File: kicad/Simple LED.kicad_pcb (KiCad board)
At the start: 2 copper layers, 100 x 60 mm, 3 parts, among them J1 Conn_01x02_Pin

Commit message: kicad schematic, 3d viewer, and files
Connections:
- net Net-(D1-K) renamed GND
- net Net-(J1-Pin_1) renamed +5V
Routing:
- added copper zone on B.Cu, net GND
- removed copper zone on B.Cu, net (none)
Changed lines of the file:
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@@
 		(tenting front back)
 		(pcbplotparams
-			(layerselection 0x00000000_00000000_55555555_5755f5ff)
+			(layerselection 0x00000000_00000000_55555555_575555ff)
 			(plot_on_all_layers_selection 0x00000000_00000000_00000000_00000000)
 			(disableapertmacros no)
@@
 			(sketchdnponfab yes)
 			(crossoutdnponfab yes)
-			(subtractmaskfromsilk no)
+			(subtractmaskfromsilk yes)
 			(outputformat 1)
 			(mirror no)
-			(drillshape 1)
+			(drillshape 0)
 			(scaleselection 1)
-			(outputdirectory "")
+			(outputdirectory "gerbers")
 		)
 	)
 	(net 0 "")
 	(net 1 "Net-(D1-A)")
-	(net 2 "Net-(D1-K)")
-	(net 3 "Net-(J1-Pin_1)")
+	(net 2 "GND")
+	(net 3 "+5V")
 	(footprint "Resistor_THT:R_Axial_DIN0617_L17.0mm_D6.0mm_P20.32mm_Horizontal"
 		(layer "F.Cu")
@@
 			(layers "*.Cu" "*.Mask")
 			(remove_unused_layers no)
-			(net 3 "Net-(J1-Pin_1)")
+			(net 3 "+5V")
 			(pintype "passive")
 		)
@@
 			(layers "*.Cu" "*.Mask")
 			(remove_unused_layers no)
-			(net 3 "Net-(J1-Pin_1)")
+			(net 3 "+5V")
 			(pinfunction "Pin_1")
 			(pintype "passive")
@@
 			(layers "*.Cu" "*.Mask")
 			(remove_unused_layers no)
-			(net 2 "Net-(D1-K)")
+			(net 2 "GND")
 			(pinfunction "Pin_2")
 			(pintype "passive")
@@
 			(layers "*.Cu" "*.Mask")
 			(remove_unused_layers no)
-			(net 2 "Net-(D1-K)")
+			(net 2 "GND")
 			(pinfunction "K")
 			(pintype "passive")
@@
 	)
 	(zone
-		(net 0)
-		(net_name "")
+		(net 2)
+		(net_name "GND")
 		(layer "B.Cu")
 		(hatch edge 0.5)
@@
 			(thermal_gap 0.5)
 			(thermal_bridge_width 0.5)
-			(island_removal_mode 1)
-			(island_area_min 10)
 		)
 		(polygon

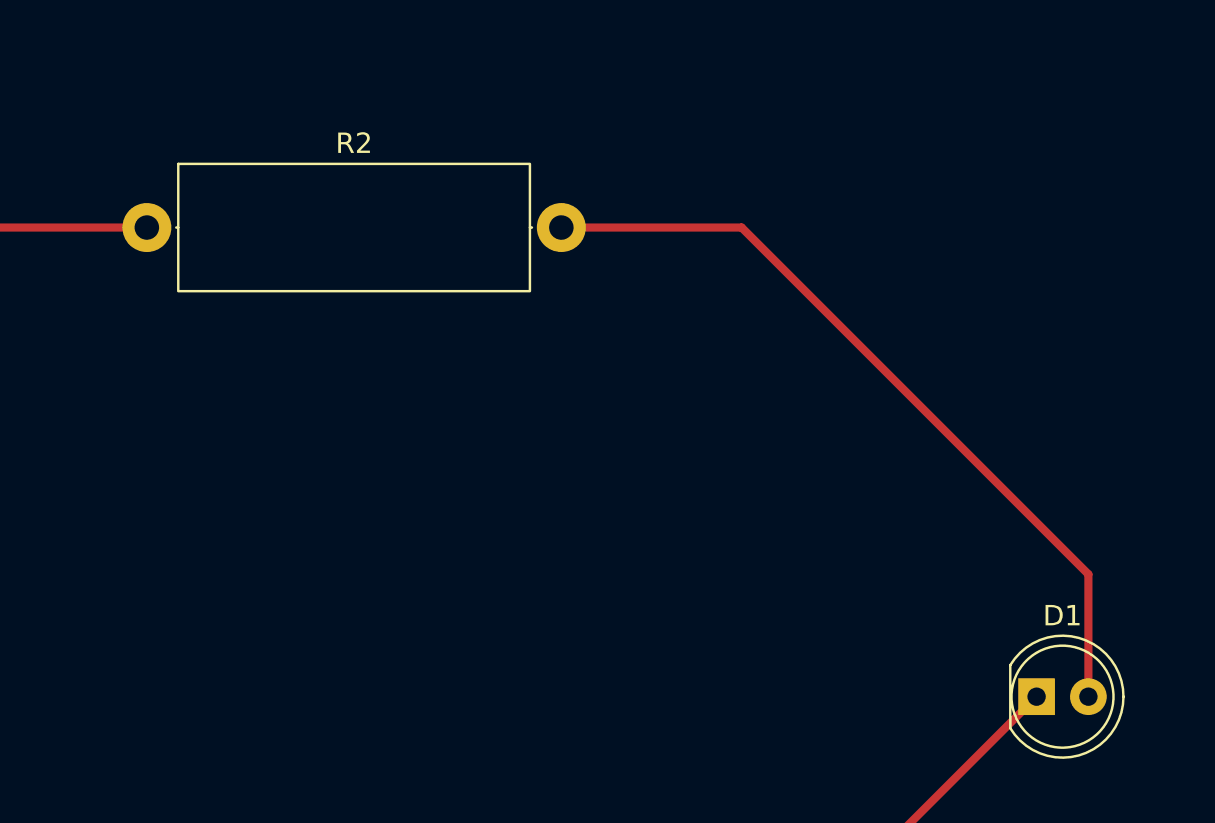
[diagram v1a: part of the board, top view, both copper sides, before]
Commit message: changed resistor footprint to the correct one
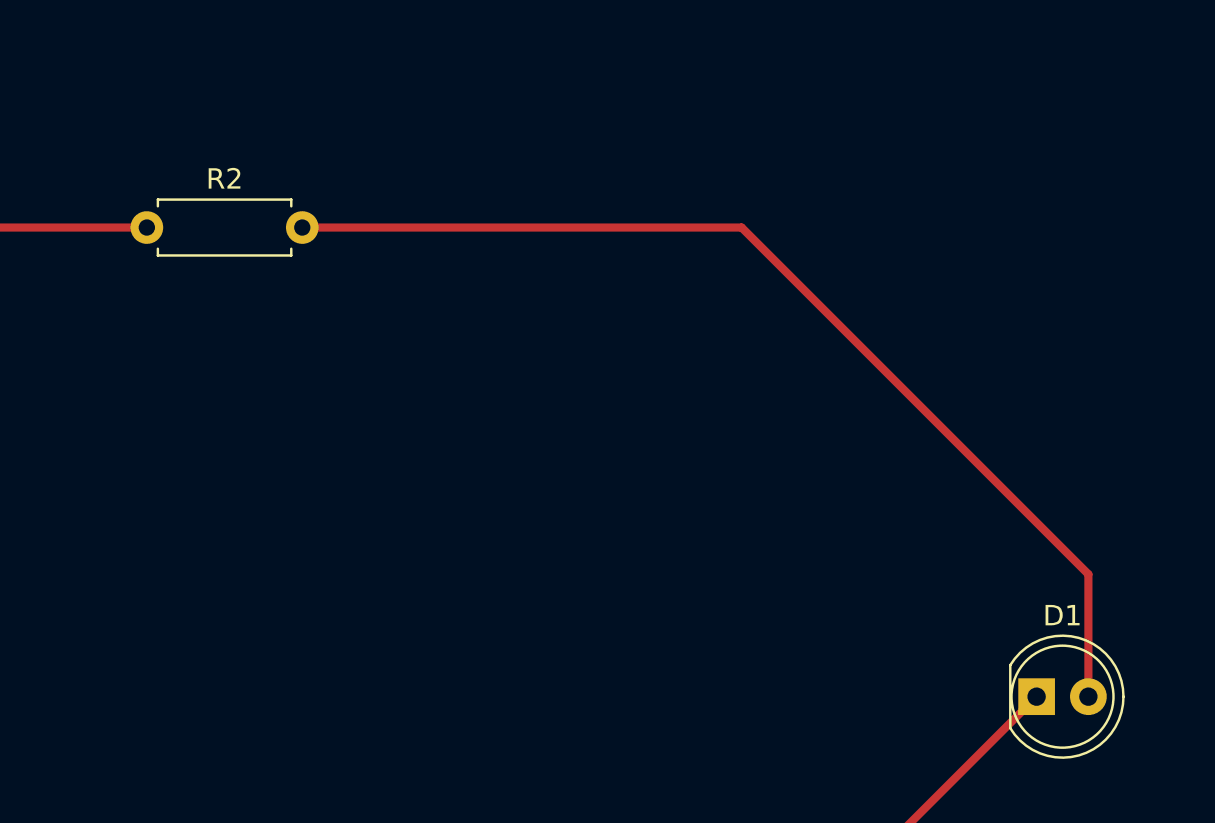
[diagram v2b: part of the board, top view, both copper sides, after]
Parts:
- R2: footprint Resistor_THT:R_Axial_DIN0617_L17.0mm_D6.0mm_P20.32mm_Horizontal -> Resistor_THT:R_Axial_DIN0207_L6.3mm_D2.5mm_P7.62mm_Horizontal
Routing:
- net Net-(D1-A): track 38.9 -> 51.6 mm
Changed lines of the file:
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@@
 	(net 2 "GND")
 	(net 3 "+5V")
-	(footprint "Resistor_THT:R_Axial_DIN0617_L17.0mm_D6.0mm_P20.32mm_Horizontal"
+	(footprint "Resistor_THT:R_Axial_DIN0207_L6.3mm_D2.5mm_P7.62mm_Horizontal"
 		(layer "F.Cu")
 		(at 140.34 93)
-		(descr "Resistor, Axial_DIN0617 series, Axial, Horizontal, pin pitch=20.32mm, 2W, length*diameter=17*6mm^2, http://www.vishay.com/docs/20128/wkxwrx.pdf")
-		(tags "Resistor Axial_DIN0617 series Axial Horizontal pin pitch 20.32mm 2W length 17mm diameter 6mm")
+		(descr "Resistor, Axial_DIN0207 series, Axial, Horizontal, pin pitch=7.62mm, 0.25W = 1/4W, length*diameter=6.3*2.5mm^2, http://cdn-reichelt.de/documents/datenblatt/B400/1_4W%23YAG.pdf")
+		(tags "Resistor Axial_DIN0207 series Axial Horizontal pin pitch 7.62mm 0.25W = 1/4W length 6.3mm diameter 2.5mm")
 		(property "Reference" "R2"
-			(at 10.16 -4.12 0)
+			(at 3.81 -2.37 0)
 			(layer "F.SilkS")
 			(effects
@@
 		)
 		(property "Value" "220"
-			(at 10.16 4.12 0)
+			(at 3.81 2.37 0)
 			(layer "F.Fab")
 			(effects
@@
 		(attr through_hole)
 		(fp_line
-			(start 1.44 0)
-			(end 1.54 0)
-			(stroke
-				(width 0.12)
-				(type solid)
-			)
-			(layer "F.SilkS")
-		)
-		(fp_line
-			(start 18.88 0)
-			(end 18.78 0)
+			(start 0.54 -1.37)
+			(end 7.08 -1.37)
+			(stroke
+				(width 0.12)
+				(type solid)
+			)
+			(layer "F.SilkS")
+		)
+		(fp_line
+			(start 0.54 -1.04)
+			(end 0.54 -1.37)
+			(stroke
+				(width 0.12)
+				(type solid)
+			)
+			(layer "F.SilkS")
+		)
+		(fp_line
+			(start 0.54 1.04)
+			(end 0.54 1.37)
+			(stroke
+				(width 0.12)
+				(type solid)
+			)
+			(layer "F.SilkS")
+		)
+		(fp_line
+			(start 0.54 1.37)
+			(end 7.08 1.37)
+			(stroke
+				(width 0.12)
+				(type solid)
+			)
+			(layer "F.SilkS")
+		)
+		(fp_line
+			(start 7.08 -1.37)
+			(end 7.08 -1.04)
+			(stroke
+				(width 0.12)
+				(type solid)
+			)
+			(layer "F.SilkS")
+		)
+		(fp_line
+			(start 7.08 1.37)
+			(end 7.08 1.04)
 			(stroke
 				(width 0.12)
@@
 		)
 		(fp_rect
-			(start 1.54 -3.12)
-			(end 18.78 3.12)
-			(stroke
-				(width 0.12)
-				(type solid)
-			)
-			(fill no)
-			(layer "F.SilkS")
-		)
-		(fp_rect
-			(start -1.45 -3.25)
-			(end 21.77 3.25)
+			(start -1.05 -1.5)
+			(end 8.67 1.5)
 			(stroke
 				(width 0.05)
@@
 		(fp_line
 			(start 0 0)
-			(end 1.66 0)
-			(stroke
-				(width 0.1)
-				(type solid)
-			)
-			(layer "F.Fab")
-		)
-		(fp_line
-			(start 20.32 0)
-			(end 18.66 0)
+			(end 0.66 0)
+			(stroke
+				(width 0.1)
+				(type solid)
+			)
+			(layer "F.Fab")
+		)
+		(fp_line
+			(start 7.62 0)
+			(end 6.96 0)
 			(stroke
 				(width 0.1)
@@
 		)
 		(fp_rect
-			(start 1.66 -3)
-			(end 18.66 3)
+			(start 0.66 -1.25)
+			(end 6.96 1.25)
 			(stroke
 				(width 0.1)
@@
 		)
 		(fp_text user "${REFERENCE}"
-			(at 10.16 0 0)
+			(at 3.81 0 0)
 			(layer "F.Fab")
 			(effects
@@
 		(pad "1" thru_hole circle
 			(at 0 0)
-			(size 2.4 2.4)
-			(drill 1.2)
+			(size 1.6 1.6)
+			(drill 0.8)
 			(layers "*.Cu" "*.Mask")
 			(remove_unused_layers no)
@@
 		)
 		(pad "2" thru_hole circle
-			(at 20.32 0)
-			(size 2.4 2.4)
-			(drill 1.2)
+			(at 7.62 0)
+			(size 1.6 1.6)
+			(drill 0.8)
 			(layers "*.Cu" "*.Mask")
 			(remove_unused_layers no)
@@
 		)
 		(embedded_fonts no)
-		(model "${KICAD9_3DMODEL_DIR}/Resistor_THT.3dshapes/R_Axial_DIN0617_L17.0mm_D6.0mm_P20.32mm_Horizontal.step"
+		(model "${KICAD9_3DMODEL_DIR}/Resistor_THT.3dshapes/R_Axial_DIN0207_L6.3mm_D2.5mm_P7.62mm_Horizontal.step"
 			(offset
 				(xyz 0 0 0)
@@
 	)
 	(segment
-		(start 169.5 93)
+		(start 186.5 116)
 		(end 186.5 110)
 		(width 0.4)
@@
 	)
 	(segment
-		(start 160.66 93)
+		(start 186.5 110)
 		(end 169.5 93)
 		(width 0.4)
@@
 	)
 	(segment
-		(start 186.5 110)
-		(end 186.5 116)
+		(start 169.5 93)
+		(end 147.96 93)
 		(width 0.4)
 		(layer "F.Cu")
